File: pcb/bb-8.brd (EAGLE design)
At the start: 128.3 x 50.8 mm, 24 parts, among them T1 2N2222, X1 STEREOJACK

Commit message: Squashed commit of the following:
commit c327650e5103bb6a6949c6a1538a163dea4dba5a
Author: Patrick Ryan <pat.m.ryan@gmail.com>
Date:   Sat Aug 20 09:49:49 2022 -0400

    Updates to PCB

commit 971e034c2edcb3dc5db781baa092387508605f21
Author: Patrick Ryan <pat.m.ryan@gmail.com>
Date:   Sat Aug 20 09:49:32 2022 -0400

    Splitting up main drive into separate files

commit 5c3a9991173692b4d5a5e5dc78048e5e86c772e9
Author: Patrick Ryan <pat.m.ryan@gmail.com>
Date:   Fri Jul 1 13:35:34 2022 -0400

    Splitting up drive functions into separate files
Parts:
- removed 7.2V: 1X2-3.5MM, adafruit:1X2-3.5MM
- removed SERVO1, SERVO2: (no value), pinhead:1X03
- removed U$4, U$5: KEYSTONE_3568, BB8:KEYSTONE_3568
- added 12V, 7V2: 1X2-3.5MM, adafruit:1X2-3.5MM
- added IC1: 786TV, linear:TO220V
- added JP2: (no value), pinhead:1X04
- added JP3, JP4: (no value), pinhead:1X08
- moved 5V 94.0 mm to (109.2, 19.1), turned to 270 degrees
- moved DOME_POT 62.5 mm to (77.5, 59.7), turned to 180 degrees
- moved U$1 47.3 mm to (59.7, 36.8), turned to 0 degrees
- moved R3 31.1 mm to (34.3, 14.0), turned to 270 degrees
- moved T1 25.0 mm to (21.6, 14.0), turned to 90 degrees
- moved DOME 23.0 mm to (66.0, 59.7), turned to 0 degrees
- moved S2S 21.7 mm to (52.1, 59.7)
- moved SBUS 21.7 mm to (109.2, 8.89), turned to 90 degrees
- moved U$3 21.6 mm to (81.3, 52.1)
- moved U$7 21.6 mm to (30.5, 26.7)
- moved FLY 20.5 mm to (36.8, 59.7)
- moved MAIN 19.2 mm to (21.6, 59.7)
- moved R1 19.1 mm to (26.7, 14.0), turned to 270 degrees
- moved R2 15.5 mm to (30.5, 14.0), turned to 270 degrees
- moved U$2 15.3 mm to (20.3, 24.1)
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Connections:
- removed net N$20: 5V.1, U$4.2A
- removed net N$21: 7.2V.1, U$5.2A
- new net +12V: 12V.1, IC1.1, JP3.1, JP4.1, SBUS.2
- new net 5V_RAW: IC1.3, R2.2
- net +5V: now also 5V.1, JP2.1, JP3.2, JP3.3, JP4.2, JP4.3; no longer R2.2, SBUS.2, U$4.1A
- net +7V: now also 7V2.1, JP3.4, JP4.4; no longer SERVO1.2, SERVO2.2, U$5.1A
- net GND: now also 12V.2, 7V2.2, IC1.2, JP2.4, JP3.5, JP3.6, JP3.7, JP3.8, JP4.5, JP4.6, JP4.7, JP4.8; no longer 7.2V.2, SERVO1.3, SERVO2.3
- net SCL: now also JP2.3
- net SDA: now also JP2.2
- net SERVO_1: no longer SERVO1.1
- net SERVO_2: no longer SERVO2.1
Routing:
- net GND: track 196.5 -> 344.4 mm, vias 1 -> 0
- net BUSY: track 155.9 -> 20.0 mm
- net 5V_RAW: track 0.00 -> 100.3 mm
- net SPK: track 120.4 -> 32.8 mm, vias 1 -> 0
- net SCL: track 18.7 -> 97.7 mm
- net DOME_POT: track 27.3 -> 94.7 mm
- net SDA: track 25.6 -> 90.2 mm, vias 1 -> 0
- net RX1: track 77.1 -> 15.6 mm, vias 1 -> 0
- net +5V: track 207.2 -> 263.4 mm
- net +12V: track 0.00 -> 55.2 mm
- net TX1: track 91.0 -> 43.9 mm, vias 1 -> 0
- net S2S_EN: track 0.65 -> 34.9 mm
- net MAIN_EN: track 31.9 -> 64.2 mm, vias 1 -> 0
- net N$6: track 44.2 -> 75.8 mm
- net +7V: track 102.6 -> 131.0 mm, vias 1 -> 0
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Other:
- board size 128.3 x 50.8 mm -> 115.6 x 64.8 mm
- board text added: "12V"
- board text added: "5V"
- board text added: "7.2V"
- board text added: "7V"
- board text added: "BATT"
- board text added: "SCL"
- board text added: "SDA"
- board text added: "SERVOS"
- board text removed: "5v"

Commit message: Updates to board
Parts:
- removed 12V: 1X2-3.5MM, adafruit:1X2-3.5MM
- removed IC1: 786TV, linear:TO220V
- removed JP1: (no value), pinhead:1X03
- removed JP2: (no value), pinhead:1X04
- removed JP3, JP4: (no value), pinhead:1X08
- added C1: 0.22uF, rcl:C050-024X044
- moved SBUS 101.5 mm to (8.89, 24.1)
- moved 5V 41.9 mm to (99.1, 59.7), turned to 0 degrees
- moved 7V2 36.6 mm to (88.9, 59.7), turned to 0 degrees
- moved DOME 11.4 mm to (54.6, 59.7)
- moved FLY 11.4 mm to (25.4, 59.7)
- moved MAIN 11.4 mm to (10.2, 59.7)
- moved S2S 11.4 mm to (40.6, 59.7)
- moved DOME_POT 8.89 mm to (68.6, 59.7)
- moved R3 2.54 mm to (31.8, 14.0)
- moved R2 1.27 mm to (29.2, 14.0)
- moved X1 1.27 mm to (3.81, 11.4)
- moved U$3 1.27 mm to (82.5, 52.1)
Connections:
- removed net +12V: 12V.1, IC1.1, JP3.1, JP4.1, SBUS.2
- removed net 5V_RAW: IC1.3, R2.2
- removed net SERVO_1: U$7.5
- removed net SERVO_2: U$7.4
- net +5V: now also R2.2; no longer JP2.1, JP3.2, JP3.3, JP4.2, JP4.3
- net +7V: now also SBUS.2; no longer JP3.4, JP4.4
- net DAC_R: no longer JP1.3
- net GND: now also C1.2; no longer 12V.2, IC1.2, JP1.2, JP2.4, JP3.5, JP3.6, JP3.7, JP3.8, JP4.5, JP4.6, JP4.7, JP4.8
- net N$6: no longer JP1.1
- net S2S_POT: now also C1.1
- net SCL: no longer JP2.3
- net SDA: no longer JP2.2
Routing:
- net GND: track 344.4 -> 0.00 mm
- net +5V: track 263.4 -> 0.00 mm
- net +7V: track 131.0 -> 0.00 mm
- net 5V_RAW: track 100.3 -> 0.00 mm
- net SCL: track 97.7 -> 0.00 mm
- net DOME_POT: track 94.7 -> 0.00 mm
- net N$5: track 92.5 -> 0.00 mm, vias 1 -> 0
- net SDA: track 90.2 -> 0.00 mm
- net N$6: track 75.8 -> 0.00 mm
- net MAIN_EN: track 64.2 -> 0.00 mm
- net DAC_R: track 60.1 -> 0.00 mm
- net IN3: track 57.6 -> 0.00 mm
- net +12V: track 55.2 -> 0.00 mm
- net SBUS: track 53.0 -> 0.00 mm
- net IN4: track 51.7 -> 0.00 mm
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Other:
- board size 115.6 x 64.8 mm -> 108 x 64.8 mm
- board text removed: "12V"
- board text removed: "7V"
- board text removed: "AUDIO"
- board text removed: "BATT"
- board text removed: "GND"
- board text removed: "SCL"
- board text removed: "SDA"
- board text removed: "SERVOS"

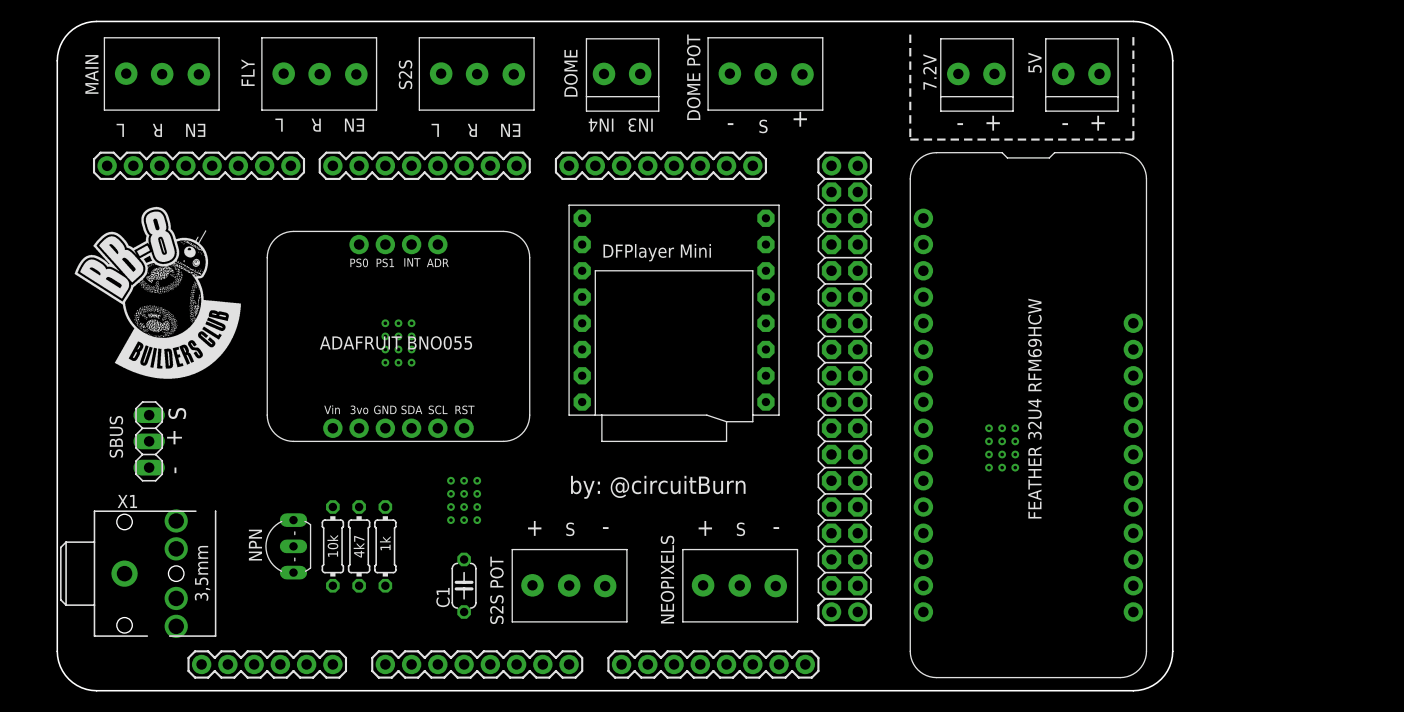
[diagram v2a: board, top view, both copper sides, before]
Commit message: Updating PCB
- Removing I2C lines
- Fixing PCB power issues
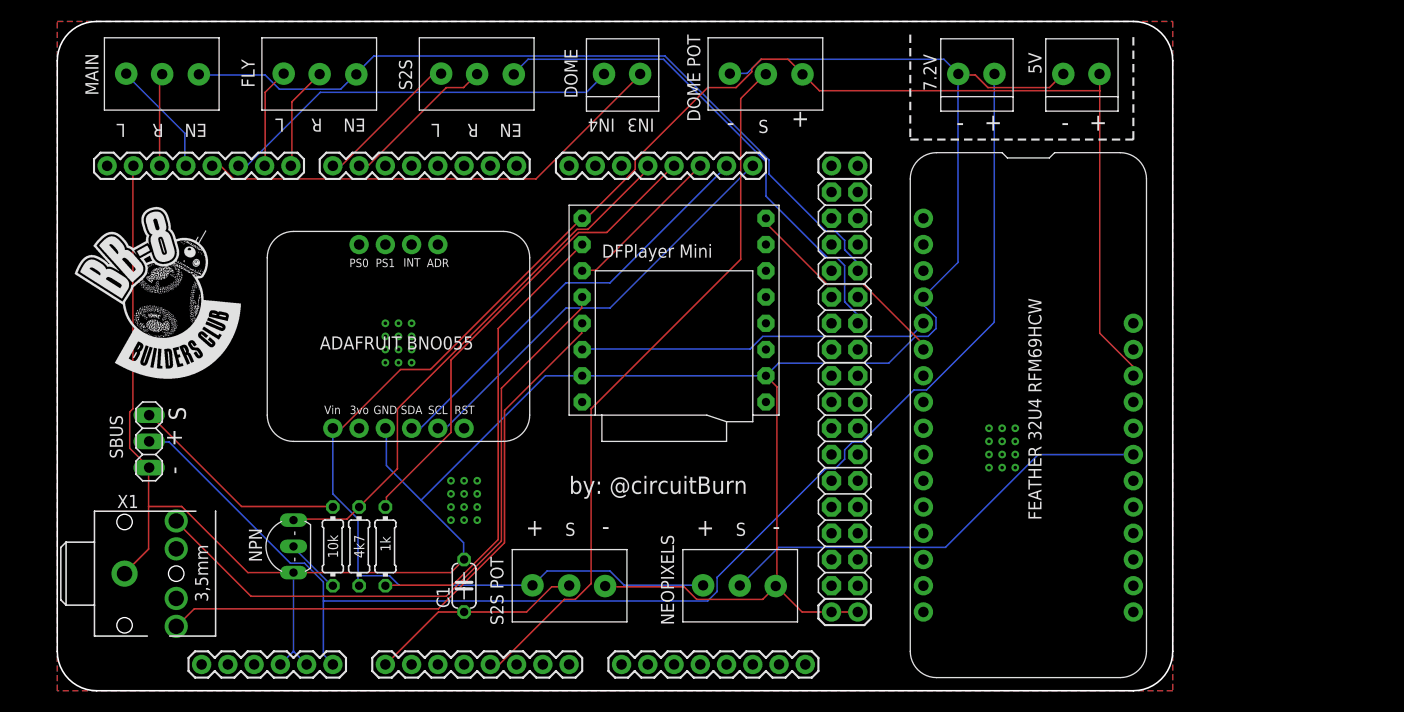
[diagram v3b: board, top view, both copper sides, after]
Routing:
- net GND: track 0.00 -> 267.3 mm
- net +5V: track 0.00 -> 172.8 mm
- net +7V: track 0.00 -> 132.3 mm
- net MAIN_EN: track 0.00 -> 76.1 mm
- net DOME_POT: track 0.00 -> 69.4 mm
- net DAC_R: track 0.00 -> 63.6 mm
- net N$6: track 0.00 -> 59.5 mm
- net SBUS: track 0.00 -> 52.2 mm
- net S2S_EN: track 0.00 -> 49.0 mm
- net TX1: track 0.00 -> 46.2 mm
- net IN3: track 0.00 -> 46.2 mm
- net N$4: track 0.00 -> 44.7 mm
- net NEO: track 0.00 -> 43.3 mm
- net SDA: track 0.00 -> 41.1 mm
- net SCL: track 0.00 -> 41.0 mm
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- added copper zone on layer 1, net GND
- added copper zone on layer 16, net GND
